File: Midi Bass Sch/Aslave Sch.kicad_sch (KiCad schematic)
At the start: 5 parts

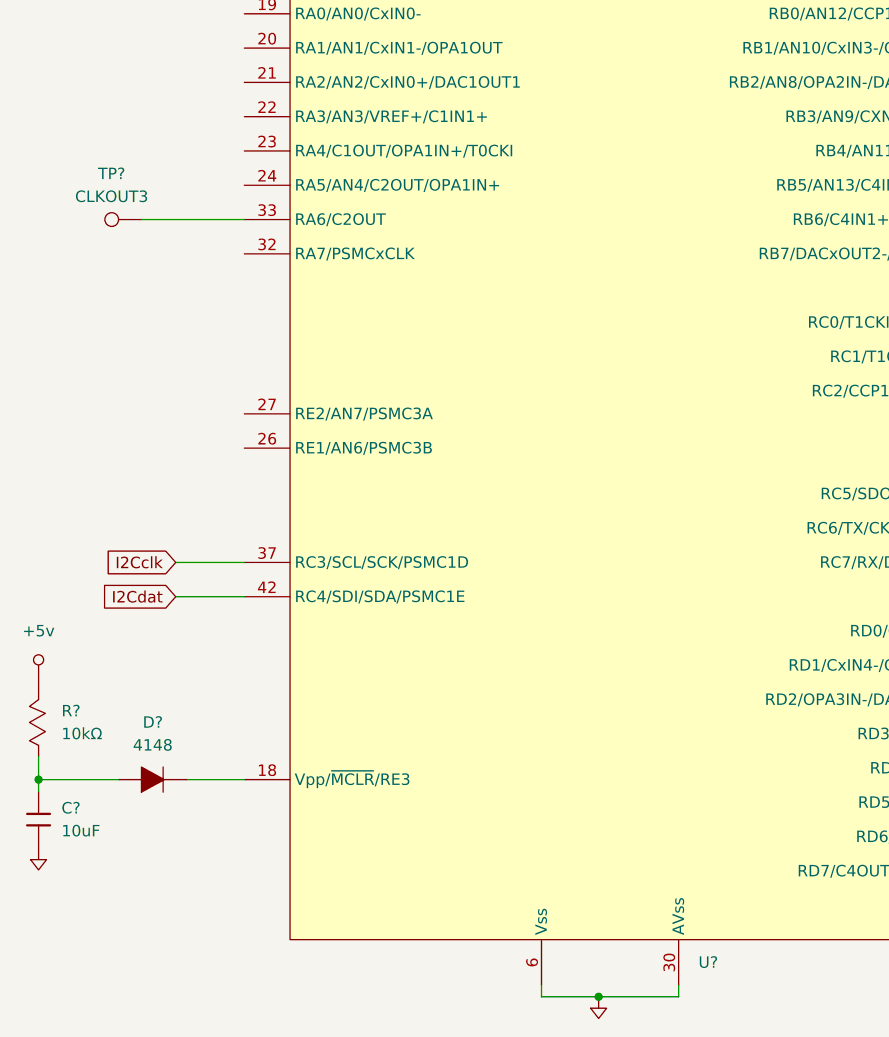
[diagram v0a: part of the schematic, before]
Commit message: updated e slave added solenoid for slave added reset button
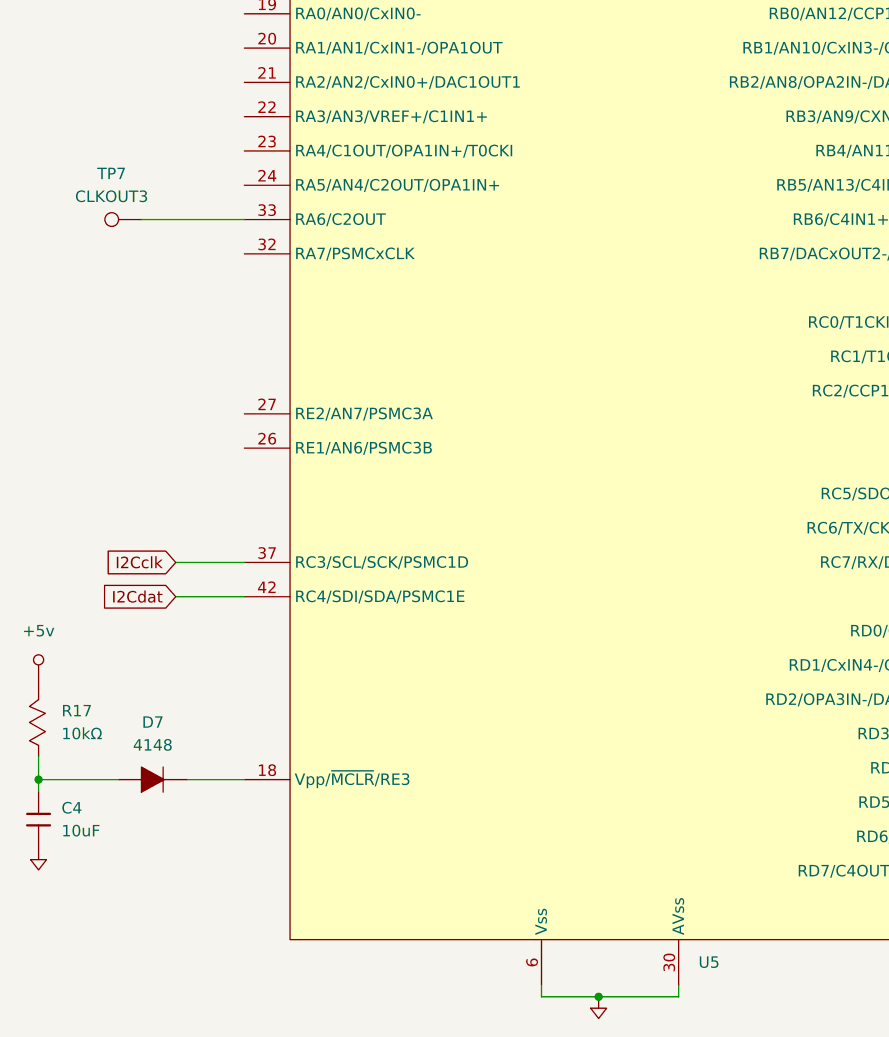
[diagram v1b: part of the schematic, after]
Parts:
- gave numbers to parts that had none: 5
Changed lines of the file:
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@@
 		(dnp no)
 		(fields_autoplaced yes)
-		(property "Reference" "U?"
+		(property "Reference" "U5"
 			(at 144.4341 152.4 0)
 			(effects
@@
 			(project "Midi Bass Sch"
 				(path "/06818073-fb22-48ee-acc5-6dedd827034e/c3b9cd48-3fcf-4fda-9d60-ef0911073906"
-					(reference "U?")
+					(reference "U5")
 					(unit 1)
 				)
@@
 		(dnp no)
 		(fields_autoplaced yes)
-		(property "Reference" "D?"
+		(property "Reference" "D7"
 			(at 83.82 125.73 90)
 			(effects
@@
 			(project "Midi Bass Sch"
 				(path "/06818073-fb22-48ee-acc5-6dedd827034e/c3b9cd48-3fcf-4fda-9d60-ef0911073906"
-					(reference "D?")
+					(reference "D7")
 					(unit 1)
 				)
@@
 		(dnp no)
 		(fields_autoplaced yes)
-		(property "Reference" "R?"
+		(property "Reference" "R17"
 			(at 73.66 124.4599 90)
 			(effects
@@
 			(project "Midi Bass Sch"
 				(path "/06818073-fb22-48ee-acc5-6dedd827034e/c3b9cd48-3fcf-4fda-9d60-ef0911073906"
-					(reference "R?")
+					(reference "R17")
 					(unit 1)
 				)
@@
 		(dnp no)
 		(fields_autoplaced yes)
-		(property "Reference" "C?"
+		(property "Reference" "C4"
 			(at 73.66 135.2549 0)
 			(effects
@@
 			(project "Midi Bass Sch"
 				(path "/06818073-fb22-48ee-acc5-6dedd827034e/c3b9cd48-3fcf-4fda-9d60-ef0911073906"
-					(reference "C?")
+					(reference "C4")
 					(unit 1)
 				)
@@
 		(dnp no)
 		(fields_autoplaced yes)
-		(property "Reference" "TP?"
+		(property "Reference" "TP7"
 			(at 79.248 64.77 90)
 			(effects
@@
 			(project "Midi Bass Sch"
 				(path "/06818073-fb22-48ee-acc5-6dedd827034e/c3b9cd48-3fcf-4fda-9d60-ef0911073906"
-					(reference "TP?")
-					(unit 1)
-				)
+					(reference "TP7")
+					(unit 1)
+				)

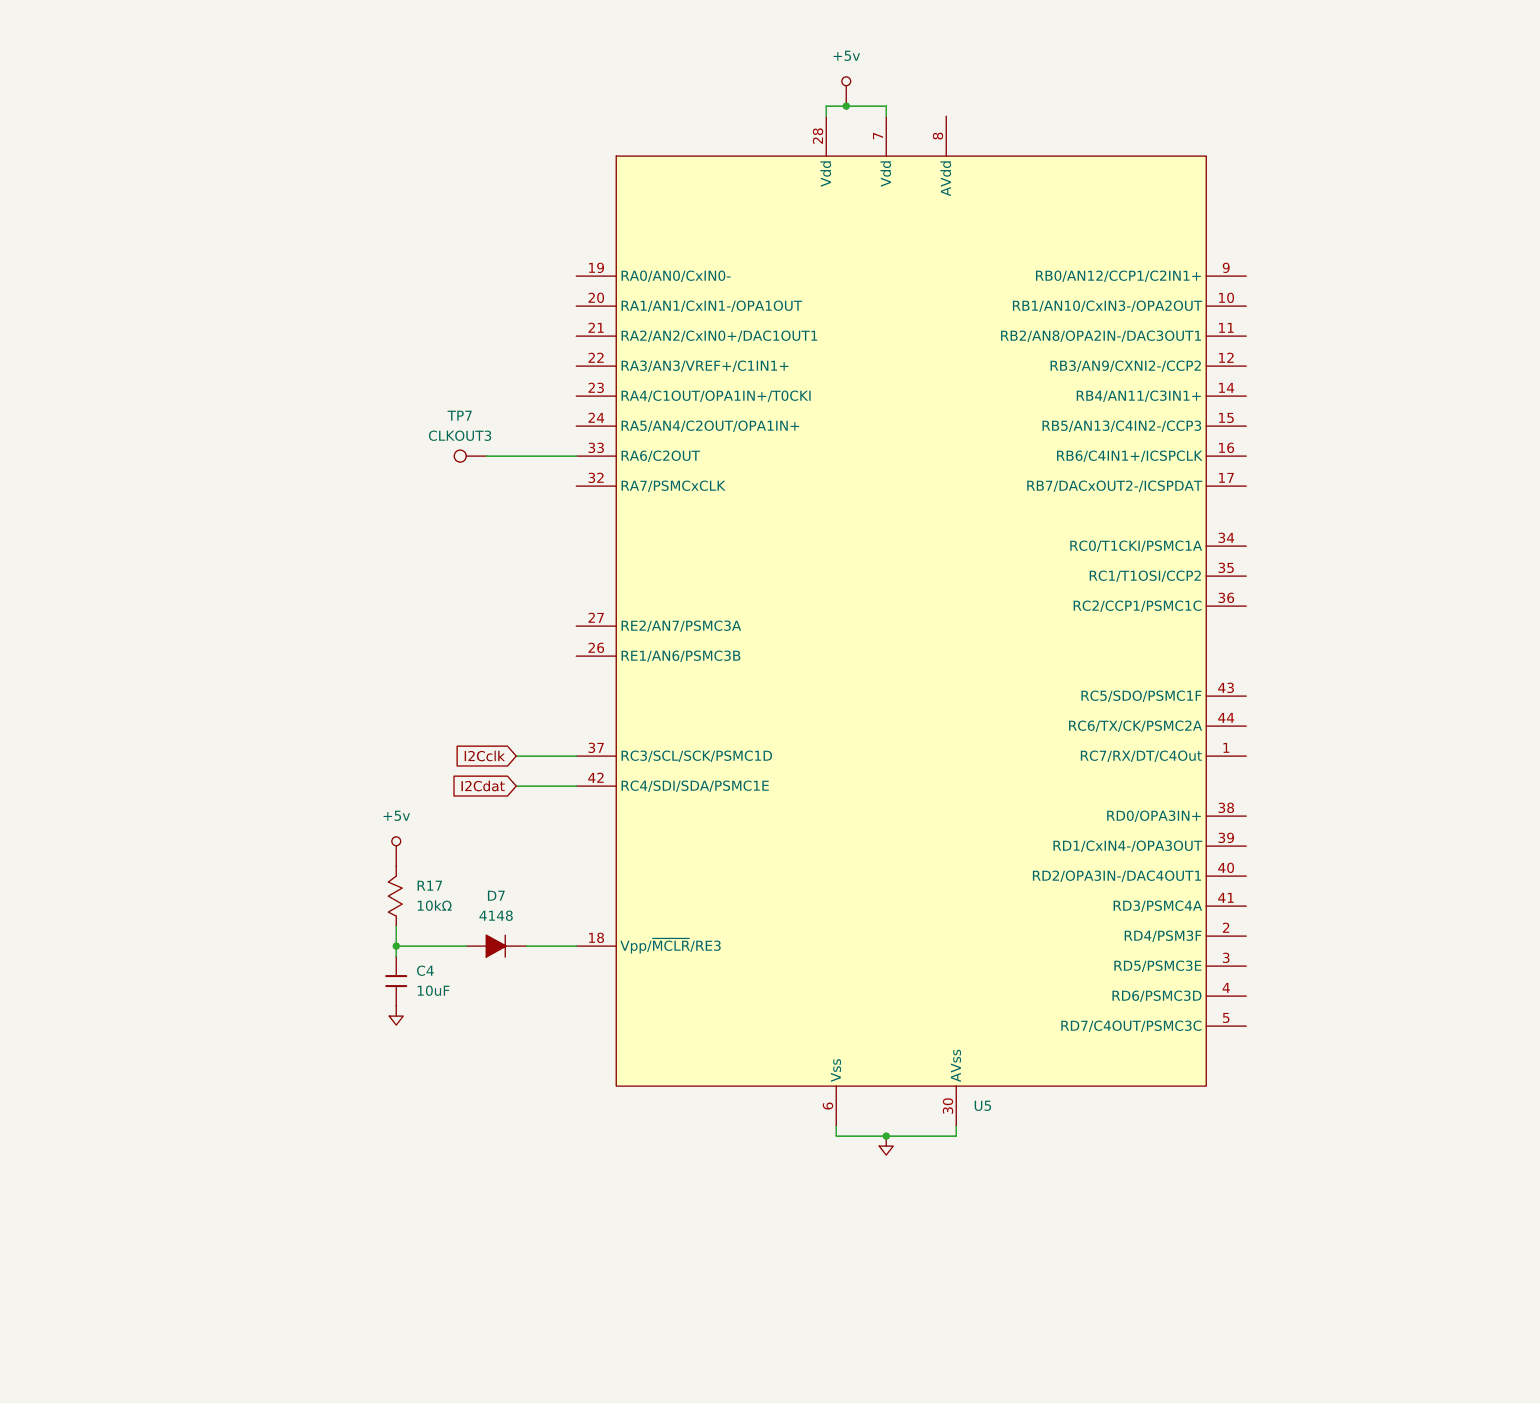
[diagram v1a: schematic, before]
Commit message: added solenoid array for the A slave
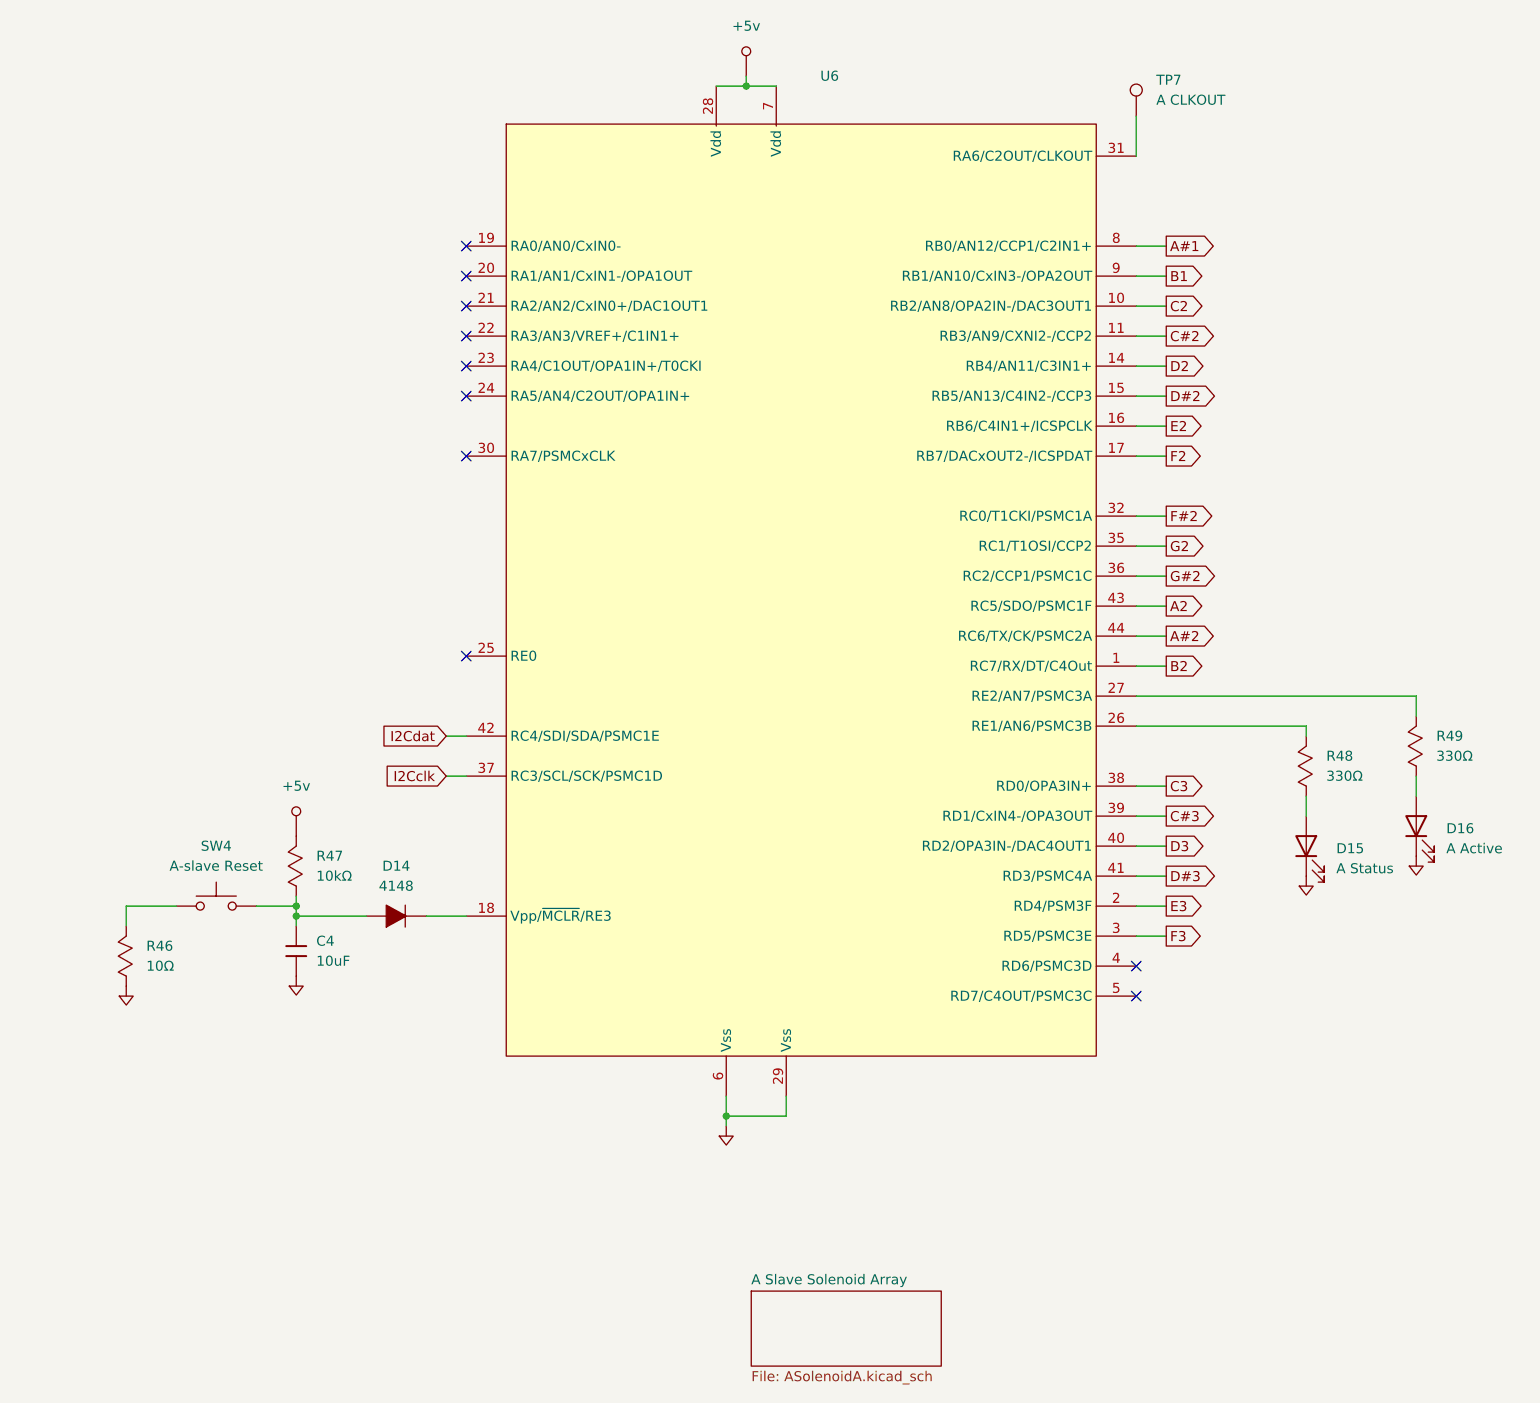
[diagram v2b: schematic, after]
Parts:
- removed D7: 4148, symbol Owen's Symbols:Diode
- removed R17: 10kΩ, symbol Owen's Symbols:Resistor_Mod
- removed U5: ~, symbol Owen's Symbols:PIC16F1789_44
- added D14: 4148, symbol Owen's Symbols:Diode
- added D15: A Status, symbol Device:LED
- added D16: A Active, symbol Device:LED
- added R46: 10Ω, symbol Owen's Symbols:Resistor_Mod
- added R47: 10kΩ, symbol Owen's Symbols:Resistor_Mod
- added R48, R49: 330Ω, symbol Owen's Symbols:Resistor_Mod
- added SW4: A-slave Reset, symbol Switch:SW_Push
- added U6: ~, symbol Owen's Symbols:PIC16F1789_44
- TP7: value CLKOUT3 -> A CLKOUT
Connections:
- net +5v: now also R47.2, U6.28 (Vdd), U6.7 (Vdd)
- net GND: now also D15.1 (K), D16.1 (K), R46.1, U6.29 (Vss), U6.6 (Vss)
- net at TP7.1: now also U6.31 (RA6/C2OUT/CLKOUT)
- net at C4.1: now also D14.1, R47.1, SW4.2
- new net: D14.2, U6.18 (Vpp/~{MCLR}/RE3)
- new net: D15.2 (A), R48.1
- new net: R48.2, U6.1 (RC7/RX/DT/C4Out)
- new net: R46.2, SW4.1
- new net: D16.2 (A), R49.1
- new net: R49.2, U6.44 (RC6/TX/CK/PSMC2A)
- new net A#1: U6.8 (RB0/AN12/CCP1/C2IN1+)
- new net A#2: U6.42 (RC4/SDI/SDA/PSMC1E)
- new net A2: U6.37 (RC3/SCL/SCK/PSMC1D)
- new net B1: U6.9 (RB1/AN10/CxIN3-/OPA2OUT)
- new net B2: U6.43 (RC5/SDO/PSMC1F)
- new net C#2: U6.11 (RB3/AN9/CXNI2-/CCP2)
- new net C#3: U6.39 (RD1/CxIN4-/OPA3OUT)
- new net C2: U6.10 (RB2/AN8/OPA2IN-/DAC3OUT1)
- new net C3: U6.38 (RD0/OPA3IN+)
- new net D#2: U6.15 (RB5/AN13/C4IN2-/CCP3)
- new net D#3: U6.41 (RD3/PSMC4A)
- new net D2: U6.14 (RB4/AN11/C3IN1+)
- new net D3: U6.40 (RD2/OPA3IN-/DAC4OUT1)
- new net E2: U6.16 (RB6/C4IN1+/ICSPCLK)
- new net E3: U6.2 (RD4/PSM3F)
- new net F#2: U6.32 (RC0/T1CKI/PSMC1A)
- new net F2: U6.17 (RB7/DACxOUT2-/ICSPDAT)
- new net F3: U6.3 (RD5/PSMC3E)
- new net G#2: U6.36 (RC2/CCP1/PSMC1C)
- new net G2: U6.35 (RC1/T1OSI/CCP2)
- no-connect marks 0 -> 10
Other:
- added sheet A Slave Solenoid Array (ASolenoidA.kicad_sch)

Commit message: added program pins to all processors
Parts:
- added J4: A SLAVE ISCP, symbol Owen's Symbols:Header_1x6
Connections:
- net +5v: now also J4.2
- net E2: now also J4.5
- net F2: now also J4.4
- net GND: now also J4.3
- net MSCLR A: now reaches D14.2, U6.18 (Vpp/~{MCLR}/RE3)
- net MSCLR A: now also J4.1
- no-connect marks 10 -> 11

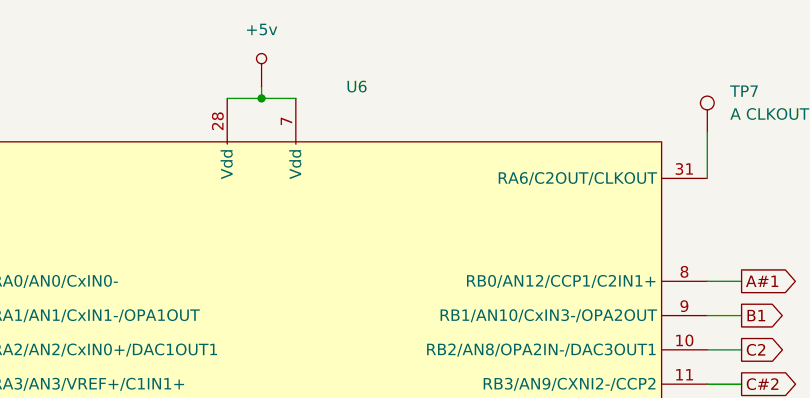
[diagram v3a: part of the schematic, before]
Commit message: added footprints to kicad schematic still need footprint for din connector
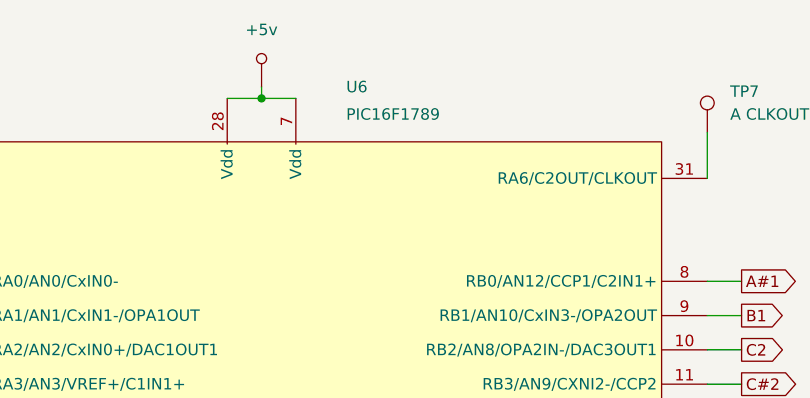
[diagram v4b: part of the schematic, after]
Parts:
- C4: footprint (none) -> Capacitor_SMD:C_0805_2012Metric_Pad1.18x1.45mm_HandSolder
- D14, D15, D16: footprint (none) -> Diode_SMD:D_0805_2012Metric_Pad1.15x1.40mm_HandSolder
- J4: footprint (none) -> Connector_PinHeader_2.54mm:PinHeader_1x06_P2.54mm_Vertical
- R46, R47, R48, R49: footprint (none) -> Resistor_SMD:R_0805_2012Metric_Pad1.20x1.40mm_HandSolder
- U6: value ~ -> PIC16F1789
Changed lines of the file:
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@@
 			)
 		)
-		(property "Footprint" ""
+		(property "Footprint" "Diode_SMD:D_0805_2012Metric_Pad1.15x1.40mm_HandSolder"
 			(at 67.31 128.27 0)
 			(effects
@@
 			)
 		)
-		(property "Footprint" ""
+		(property "Footprint" "Resistor_SMD:R_0805_2012Metric_Pad1.20x1.40mm_HandSolder"
 			(at 184.15 110.49 0)
 			(effects
@@
 			)
 		)
-		(property "Footprint" ""
+		(property "Footprint" "Resistor_SMD:R_0805_2012Metric_Pad1.20x1.40mm_HandSolder"
 			(at 34.29 134.62 0)
 			(effects
@@
 			)
 		)
-		(property "Footprint" ""
+		(property "Footprint" "Diode_SMD:D_0805_2012Metric_Pad1.15x1.40mm_HandSolder"
 			(at 200.66 116.84 0)
 			(effects
@@
 			)
 		)
-		(property "Footprint" ""
+		(property "Footprint" "Resistor_SMD:R_0805_2012Metric_Pad1.20x1.40mm_HandSolder"
 			(at 55.88 123.19 0)
 			(effects
@@
 			)
 		)
-		(property "Value" "~"
-			(at 130.4641 149.86 0)
+		(property "Value" "PIC16F1789"
+			(at 124.968 24.638 0)
 			(effects
 				(font
@@
 			)
 		)
-		(property "Footprint" ""
+		(property "Footprint" "Capacitor_SMD:C_0805_2012Metric_Pad1.18x1.45mm_HandSolder"
 			(at 58.42 127 0)
 			(effects
@@
 			)
 		)
-		(property "Footprint" ""
+		(property "Footprint" "Resistor_SMD:R_0805_2012Metric_Pad1.20x1.40mm_HandSolder"
 			(at 198.12 107.95 0)
 			(effects
@@
 			)
 		)
-		(property "Footprint" ""
+		(property "Footprint" "Connector_PinHeader_2.54mm:PinHeader_1x06_P2.54mm_Vertical"
 			(at 30.48 54.61 0)
 			(effects
@@
 			)
 		)
-		(property "Footprint" ""
+		(property "Footprint" "Diode_SMD:D_0805_2012Metric_Pad1.15x1.40mm_HandSolder"
 			(at 186.69 119.38 0)
 			(effects
